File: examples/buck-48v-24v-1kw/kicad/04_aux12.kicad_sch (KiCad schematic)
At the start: 14 parts, among them U2 LM5164DDAR

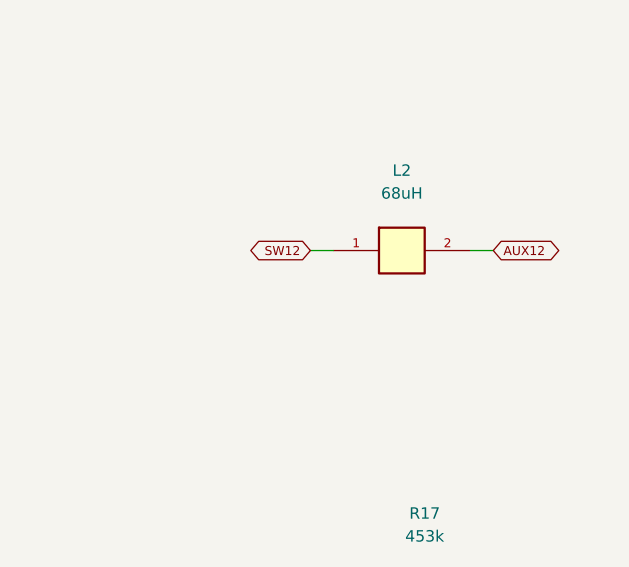
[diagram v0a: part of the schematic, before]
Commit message: feat: complete six-layer power PCB routing and pass native DRC
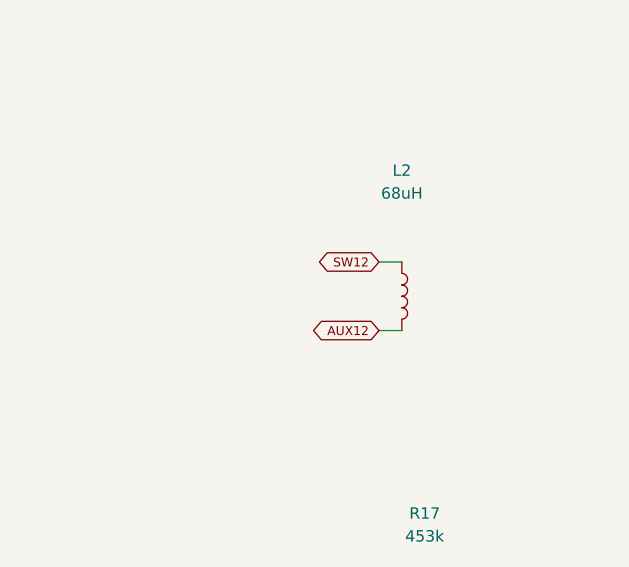
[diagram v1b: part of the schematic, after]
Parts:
- U2: footprint Package_SO:SOIC-8-1EP_3.9x4.9mm_P1.27mm_EP2.29x3mm -> Package_SO:SOIC-8-1EP_3.9x4.9mm_P1.27mm_EP2.95x4.9mm_Mask2.71x3.4mm
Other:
- moved on the sheet: L2
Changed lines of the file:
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@@
           (property "Reference" "U2" (at 68.58 34.29 0)  (effects (font (size 1.27 1.27))))
 (property "Value" "LM5164DDAR" (at 68.58 36.83 0)  (effects (font (size 1.27 1.27))))
-(property "Footprint" "Package_SO:SOIC-8-1EP_3.9x4.9mm_P1.27mm_EP2.29x3mm" (at 68.58 48.26 0) (hide yes) (effects (font (size 1.27 1.27))))
+(property "Footprint" "Package_SO:SOIC-8-1EP_3.9x4.9mm_P1.27mm_EP2.95x4.9mm_Mask2.71x3.4mm" (at 68.58 48.26 0) (hide yes) (effects (font (size 1.27 1.27))))
 (property "Datasheet" "" (at 68.58 48.26 0) (hide yes) (effects (font (size 1.27 1.27))))
           (pin "1")
@@
           (effects (font (size 1.0 1.0)) (justify left))
 )
-(symbol (lib_id "AIPE:Sym_L2") (at 353.06 43.18 0)
+(symbol (lib_id "AIPE:Sym_L2") (at 353.06 48.26 0)
           (unit 1) (in_bom yes) (on_board yes) (dnp no)
           (property "Reference" "L2" (at 353.06 34.29 0)  (effects (font (size 1.27 1.27))))
 (property "Value" "68uH" (at 353.06 36.83 0)  (effects (font (size 1.27 1.27))))
-(property "Footprint" "Inductor_SMD:L_Coilcraft_MSS1246T-XXX" (at 353.06 43.18 0) (hide yes) (effects (font (size 1.27 1.27))))
-(property "Datasheet" "" (at 353.06 43.18 0) (hide yes) (effects (font (size 1.27 1.27))))
+(property "Footprint" "Inductor_SMD:L_Coilcraft_MSS1246T-XXX" (at 353.06 48.26 0) (hide yes) (effects (font (size 1.27 1.27))))
+(property "Datasheet" "" (at 353.06 48.26 0) (hide yes) (effects (font (size 1.27 1.27))))
           (pin "1")
 (pin "2")
           (instances (project "AIPE_Buck_1kW" (path "/558e48a2-11d7-5e19-b5b7-8bc9de1ba629/ca189374-1703-55cb-b602-676b8bab71a8"
             (reference "L2") (unit 1)))))
-(wire (pts (xy 345.44 43.18) (xy 342.9 43.18))
+(wire (pts (xy 353.06 44.449999999999996) (xy 350.52 44.449999999999996))
           (stroke (width 0) (type default)))
 (global_label "SW12" (shape bidirectional)
-          (at 342.9 43.18 180)
+          (at 350.52 44.449999999999996 180)
           (effects (font (size 1.0 1.0)) (justify right))
 )
-(wire (pts (xy 360.68 43.18) (xy 363.22 43.18))
+(wire (pts (xy 353.06 52.07) (xy 350.52 52.07))
           (stroke (width 0) (type default)))
 (global_label "AUX12" (shape bidirectional)
-          (at 363.22 43.18 0)
-          (effects (font (size 1.0 1.0)) (justify left))
+          (at 350.52 52.07 180)
+          (effects (font (size 1.0 1.0)) (justify right))
 )
 (symbol (lib_id "AIPE:Sym_C35") (at 38.1 81.28000000000002 0)
